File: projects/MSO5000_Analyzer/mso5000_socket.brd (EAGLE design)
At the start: 76.7 x 38 mm, 3 parts

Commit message: Editing board
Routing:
- net !D4: track 63.4 -> 64.9 mm
- net !D5: track 65.3 -> 66.5 mm
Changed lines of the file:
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@@
 <wire x1="74.9" y1="40.5" x2="-1.3" y2="40.5" width="0" layer="20"/>
 <wire x1="-1.3" y1="40.5" x2="-1.79" y2="2.47" width="0" layer="20"/>
-<wire x1="22.7" y1="10.2" x2="22.7" y2="12.9" width="0.1524" layer="41"/>
-<wire x1="22.7" y1="12.9" x2="20.7" y2="12.9" width="0.1524" layer="41"/>
-<wire x1="20.7" y1="12.9" x2="20.7" y2="10.2" width="0.1524" layer="41"/>
-<wire x1="50.9" y1="10.1" x2="50.9" y2="12.8" width="0.1524" layer="41"/>
-<wire x1="50.9" y1="12.8" x2="48.9" y2="12.8" width="0.1524" layer="41"/>
-<wire x1="48.9" y1="12.8" x2="48.9" y2="10.1" width="0.1524" layer="41"/>
+<wire x1="22.7" y1="12.2" x2="20.7" y2="12.2" width="0.1524" layer="41"/>
+<wire x1="50.6" y1="12.2" x2="48.6" y2="12.2" width="0.1524" layer="41"/>
+<wire x1="20.7" y1="12.2" x2="20.7" y2="8.7" width="0.1524" layer="41"/>
+<wire x1="22.7" y1="12.2" x2="22.7" y2="8.7" width="0.1524" layer="41"/>
+<wire x1="48.6" y1="12.2" x2="48.6" y2="8.8" width="0.1524" layer="41"/>
+<wire x1="50.6" y1="12.2" x2="50.6" y2="8.8" width="0.1524" layer="41"/>
 </plain>
 <attributes>
@@
 <wire x1="30.06" y1="8.06" x2="30.06" y2="8.59699375" width="0.254" layer="1"/>
 <wire x1="30.06" y1="8.59699375" x2="30.06" y2="11.43" width="0.254" layer="1"/>
-<wire x1="19.5" y1="12.62591875" x2="19.5" y2="9.6" width="0.254" layer="16"/>
+<wire x1="19.5" y1="12.62591875" x2="19.5" y2="7.5" width="0.254" layer="16"/>
 <wire x1="18.05611875" y1="31.1302" x2="20.64388125" y2="31.1302" width="0.254" layer="16"/>
 <wire x1="17.4698" y1="30.54388125" x2="18.05611875" y2="31.1302" width="0.254" layer="16"/>
@@
 <wire x1="21.01439375" y1="30.7596875" x2="20.64388125" y2="31.1302" width="0.254" layer="16"/>
 <wire x1="19.5" y1="12.62591875" x2="22.087040625" y2="15.212959375" width="0.254" layer="16"/>
-<wire x1="19.5" y1="9.6" x2="22.4948875" y2="6.6051125" width="0.254" layer="16"/>
-<wire x1="22.4948875" y1="6.6051125" x2="27.4051125" y2="6.6051125" width="0.254" layer="16"/>
+<wire x1="19.5" y1="7.5" x2="20.3948875" y2="6.6051125" width="0.254" layer="16"/>
+<wire x1="20.3948875" y1="6.6051125" x2="27.4051125" y2="6.6051125" width="0.254" layer="16"/>
 <wire x1="22.087040625" y1="15.212959375" x2="22.087040625" y2="25.153634375" width="0.254" layer="16"/>
 <wire x1="22.087040625" y1="25.153634375" x2="18.436475" y2="28.8042" width="0.254" layer="16"/>
@@
 <wire x1="20.8" y1="15.3" x2="20.375734375" y2="14.875734375" width="0.254" layer="1"/>
 <wire x1="20.375734375" y1="14.875734375" x2="19.3" y2="13.8" width="0.254" layer="1"/>
-<wire x1="19.3" y1="13.8" x2="19.3" y2="9.8" width="0.254" layer="1"/>
+<wire x1="19.3" y1="13.8" x2="19.3" y2="7.3" width="0.254" layer="1"/>
 <wire x1="29.06" y1="8.66" x2="29.06" y2="11.43" width="0.254" layer="1"/>
 <wire x1="24.13" y1="34.43" x2="22.9" y2="33.2" width="0.254" layer="16"/>
 <wire x1="16.9958" y1="30.84021875" x2="16.9958" y2="28.9042" width="0.254" layer="16"/>
-<wire x1="19.3" y1="9.8" x2="23.0948875" y2="6.0051125" width="0.254" layer="1"/>
-<wire x1="23.0948875" y1="6.0051125" x2="26.4051125" y2="6.0051125" width="0.254" layer="1"/>
+<wire x1="19.3" y1="7.3" x2="20.5948875" y2="6.0051125" width="0.254" layer="1"/>
+<wire x1="20.5948875" y1="6.0051125" x2="26.4051125" y2="6.0051125" width="0.254" layer="1"/>
 <wire x1="26.4051125" y1="6.0051125" x2="29.06" y2="8.66" width="0.254" layer="1"/>
 <wire x1="21.6" y1="24.8703375" x2="21.6" y2="16.1" width="0.254" layer="16"/>

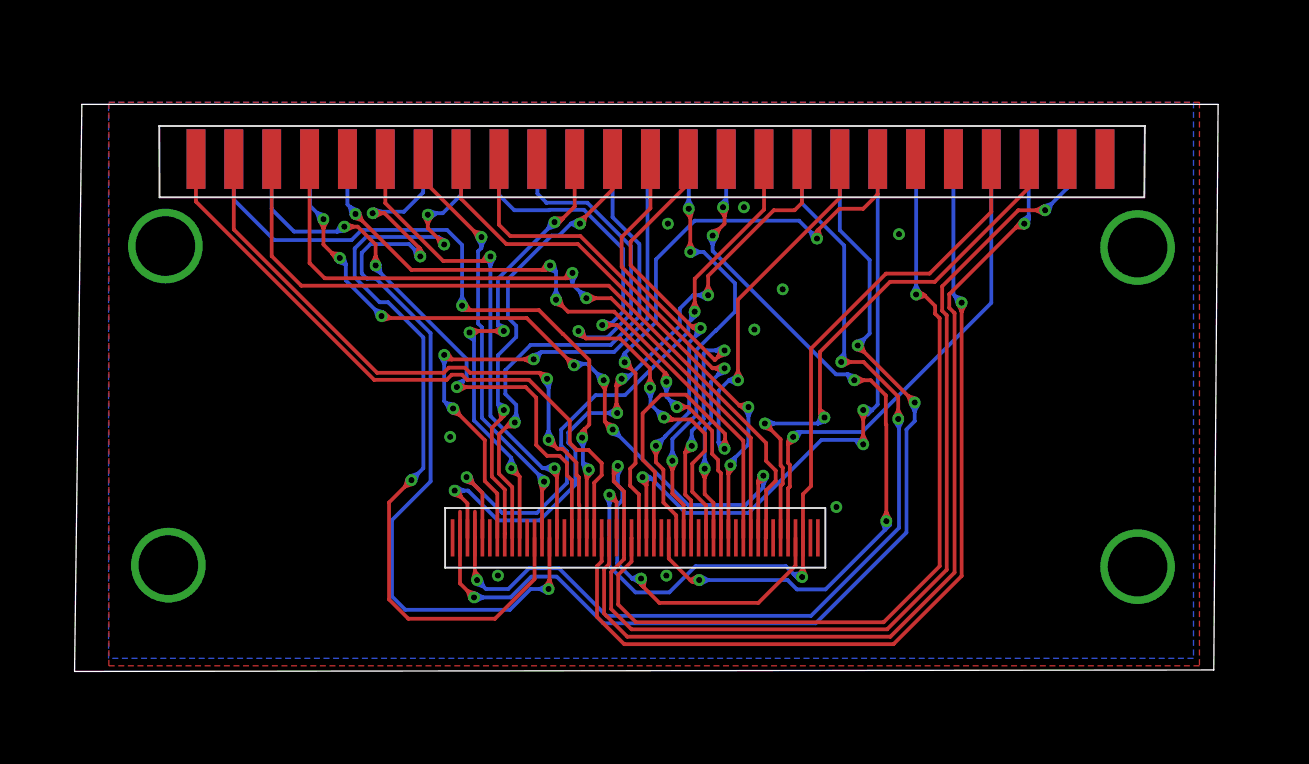
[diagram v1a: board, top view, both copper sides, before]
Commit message: Editing Area Top and Bottom. Adding extra calibration point's
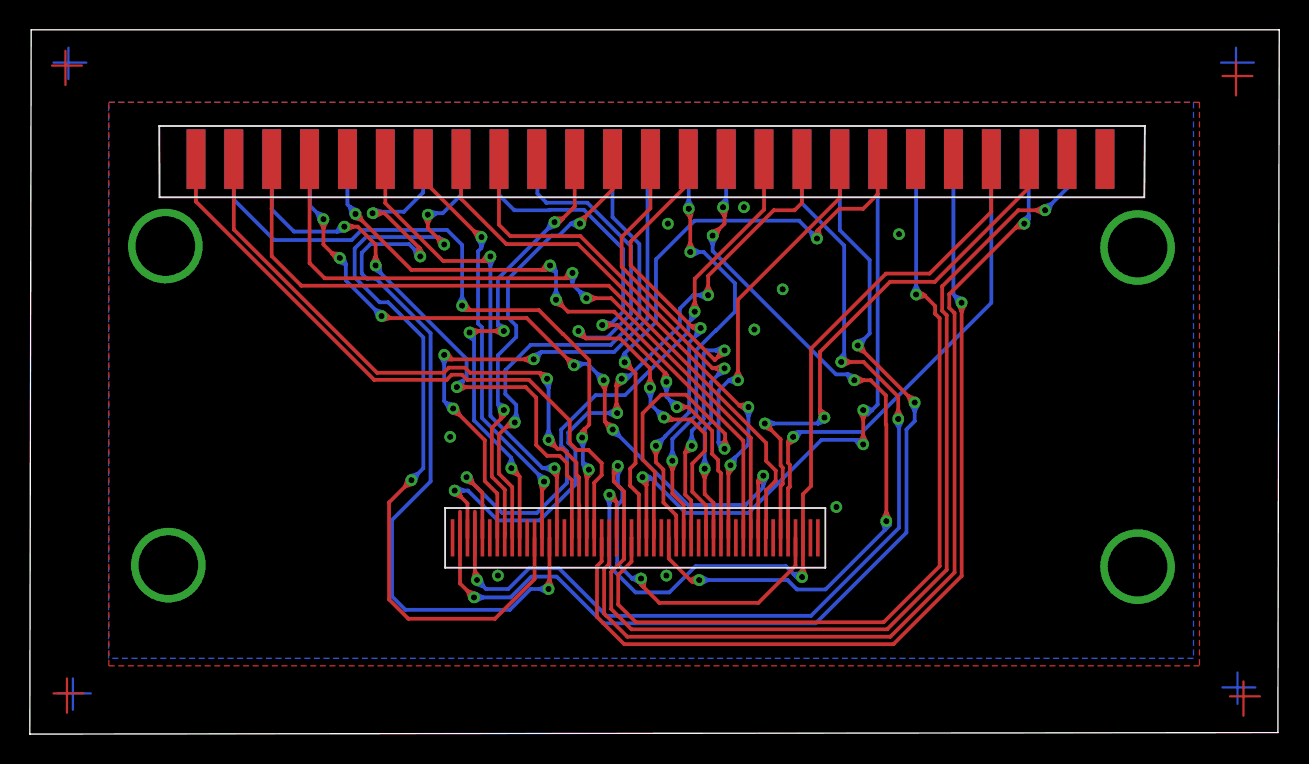
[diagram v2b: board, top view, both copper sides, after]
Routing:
- net N$5: track 0.00 -> 2.30 mm
- net N$9: track 0.00 -> 2.30 mm
- net N$11: track 0.00 -> 2.30 mm
- net N$7: track 0.00 -> 2.30 mm
- net N$18: track 0.00 -> 2.20 mm
- net N$16: track 0.00 -> 2.20 mm
- net N$20: track 0.00 -> 2.20 mm
- net N$14: track 0.00 -> 2.20 mm
- net N$19: track 0.00 -> 2.10 mm
- net N$17: track 0.00 -> 2.10 mm
- net N$15: track 0.00 -> 2.10 mm
- net N$13: track 0.00 -> 2.10 mm
- net N$8: track 0.00 -> 2.00 mm
- net N$12: track 0.00 -> 2.00 mm
- net N$10: track 0.00 -> 2.00 mm
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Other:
- board size 76.7 x 38 mm -> 83.8 x 47.2 mm
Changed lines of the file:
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@@
 <grid distance="0.1" unitdist="mm" unit="mm" style="lines" multiple="1" display="no" altdistance="0.01" altunitdist="mm" altunit="mm"/>
 <layers>
-<layer number="1" name="Top" color="4" fill="1" visible="yes" active="yes"/>
+<layer number="1" name="Top" color="4" fill="1" visible="no" active="yes"/>
 <layer number="2" name="Route2" color="16" fill="1" visible="no" active="no"/>
 <layer number="3" name="Route3" color="17" fill="1" visible="no" active="no"/>
@@
 <board>
 <plain>
-<wire x1="-1.79" y1="2.47" x2="74.61" y2="2.57" width="0" layer="20"/>
-<wire x1="74.61" y1="2.57" x2="74.9" y2="40.5" width="0" layer="20"/>
-<wire x1="74.9" y1="40.5" x2="-1.3" y2="40.5" width="0" layer="20"/>
-<wire x1="-1.3" y1="40.5" x2="-1.79" y2="2.47" width="0" layer="20"/>
+<wire x1="-4.79" y1="-1.73" x2="78.91" y2="-1.63" width="0" layer="20"/>
+<wire x1="78.91" y1="-1.63" x2="79" y2="45.5" width="0" layer="20"/>
+<wire x1="79" y1="45.5" x2="-4.7" y2="45.5" width="0" layer="20"/>
+<wire x1="-4.7" y1="45.5" x2="-4.79" y2="-1.73" width="0" layer="20"/>
 <wire x1="22.7" y1="12.2" x2="20.7" y2="12.2" width="0.1524" layer="41"/>
 <wire x1="50.6" y1="12.2" x2="48.6" y2="12.2" width="0.1524" layer="41"/>
@@
 <via x="69.5" y="30.9" extent="1-16" drill="4"/>
 </signal>
+<signal name="N$7">
+<wire x1="76.1" y1="43.4" x2="76.1" y2="41.1" width="0.1524" layer="1"/>
+</signal>
+<signal name="N$8">
+<wire x1="75.2" y1="42.4" x2="77.2" y2="42.4" width="0.1524" layer="1"/>
+</signal>
+<signal name="N$9">
+<wire x1="-2.3" y1="2" x2="-2.3" y2="-0.3" width="0.1524" layer="1"/>
+</signal>
+<signal name="N$10">
+<wire x1="-3.2" y1="1" x2="-1.2" y2="1" width="0.1524" layer="1"/>
+</signal>
+<signal name="N$11">
+<wire x1="76.6" y1="1.8" x2="76.6" y2="-0.5" width="0.1524" layer="1"/>
+</signal>
+<signal name="N$12">
+<wire x1="75.7" y1="0.8" x2="77.7" y2="0.8" width="0.1524" layer="1"/>
+</signal>
+<signal name="N$5">
+<wire x1="-2.4" y1="44.1" x2="-2.4" y2="41.8" width="0.1524" layer="1"/>
+</signal>
+<signal name="N$6">
+<wire x1="-3.3" y1="43.1" x2="-1.3" y2="43.1" width="0.1524" layer="1"/>
+</signal>
+<signal name="N$15">
+<wire x1="76.1" y1="44.3" x2="76.1" y2="42.2" width="0.1524" layer="16"/>
+</signal>
+<signal name="N$16">
+<wire x1="75.1" y1="43.3" x2="77.3" y2="43.3" width="0.1524" layer="16"/>
+</signal>
+<signal name="N$17">
+<wire x1="76.2" y1="2.4" x2="76.2" y2="0.3" width="0.1524" layer="16"/>
+</signal>
+<signal name="N$18">
+<wire x1="75.2" y1="1.4" x2="77.4" y2="1.4" width="0.1524" layer="16"/>
+</signal>
+<signal name="N$19">
+<wire x1="-1.9" y1="2" x2="-1.9" y2="-0.1" width="0.1524" layer="16"/>
+</signal>
+<signal name="N$20">
+<wire x1="-2.9" y1="1" x2="-0.7" y2="1" width="0.1524" layer="16"/>
+</signal>
+<signal name="N$13">
+<wire x1="-2.2" y1="44.3" x2="-2.2" y2="42.2" width="0.1524" layer="16"/>
+</signal>
+<signal name="N$14">
+<wire x1="-3.2" y1="43.3" x2="-1" y2="43.3" width="0.1524" layer="16"/>
+</signal>
 </signals>
 <mfgpreviewcolors>
@@
 <mfgpreviewcolor name="substratecolor" color="0xFF786E46"/>
 </mfgpreviewcolors>
+<errors>
+</errors>
 </board>
 </drawing>

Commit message: Editing board
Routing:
- net N$5: track 2.30 -> 0.00 mm
- net N$9: track 2.30 -> 0.00 mm
- net N$11: track 2.30 -> 0.00 mm
- net N$7: track 2.30 -> 0.00 mm
- net N$18: track 2.20 -> 0.00 mm
- net N$16: track 2.20 -> 0.00 mm
- net N$20: track 2.20 -> 0.00 mm
- net N$14: track 2.20 -> 0.00 mm
- net N$19: track 2.10 -> 0.00 mm
- net N$17: track 2.10 -> 0.00 mm
- net N$15: track 2.10 -> 0.00 mm
- net N$13: track 2.10 -> 0.00 mm
- net N$8: track 2.00 -> 0.00 mm
- net N$12: track 2.00 -> 0.00 mm
- net N$10: track 2.00 -> 0.00 mm
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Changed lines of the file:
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@@
 <grid distance="0.1" unitdist="mm" unit="mm" style="lines" multiple="1" display="no" altdistance="0.01" altunitdist="mm" altunit="mm"/>
 <layers>
-<layer number="1" name="Top" color="4" fill="1" visible="no" active="yes"/>
+<layer number="1" name="Top" color="4" fill="1" visible="yes" active="yes"/>
 <layer number="2" name="Route2" color="16" fill="1" visible="no" active="no"/>
 <layer number="3" name="Route3" color="17" fill="1" visible="no" active="no"/>
@@
 <via x="69.5" y="30.9" extent="1-16" drill="4"/>
 </signal>
-<signal name="N$7">
-<wire x1="76.1" y1="43.4" x2="76.1" y2="41.1" width="0.1524" layer="1"/>
-</signal>
-<signal name="N$8">
-<wire x1="75.2" y1="42.4" x2="77.2" y2="42.4" width="0.1524" layer="1"/>
-</signal>
-<signal name="N$9">
-<wire x1="-2.3" y1="2" x2="-2.3" y2="-0.3" width="0.1524" layer="1"/>
-</signal>
-<signal name="N$10">
-<wire x1="-3.2" y1="1" x2="-1.2" y2="1" width="0.1524" layer="1"/>
-</signal>
-<signal name="N$11">
-<wire x1="76.6" y1="1.8" x2="76.6" y2="-0.5" width="0.1524" layer="1"/>
-</signal>
-<signal name="N$12">
-<wire x1="75.7" y1="0.8" x2="77.7" y2="0.8" width="0.1524" layer="1"/>
-</signal>
-<signal name="N$5">
-<wire x1="-2.4" y1="44.1" x2="-2.4" y2="41.8" width="0.1524" layer="1"/>
-</signal>
-<signal name="N$6">
-<wire x1="-3.3" y1="43.1" x2="-1.3" y2="43.1" width="0.1524" layer="1"/>
-</signal>
-<signal name="N$15">
-<wire x1="76.1" y1="44.3" x2="76.1" y2="42.2" width="0.1524" layer="16"/>
-</signal>
-<signal name="N$16">
-<wire x1="75.1" y1="43.3" x2="77.3" y2="43.3" width="0.1524" layer="16"/>
-</signal>
-<signal name="N$17">
-<wire x1="76.2" y1="2.4" x2="76.2" y2="0.3" width="0.1524" layer="16"/>
-</signal>
-<signal name="N$18">
-<wire x1="75.2" y1="1.4" x2="77.4" y2="1.4" width="0.1524" layer="16"/>
-</signal>
-<signal name="N$19">
-<wire x1="-1.9" y1="2" x2="-1.9" y2="-0.1" width="0.1524" layer="16"/>
-</signal>
-<signal name="N$20">
-<wire x1="-2.9" y1="1" x2="-0.7" y2="1" width="0.1524" layer="16"/>
-</signal>
-<signal name="N$13">
-<wire x1="-2.2" y1="44.3" x2="-2.2" y2="42.2" width="0.1524" layer="16"/>
-</signal>
-<signal name="N$14">
-<wire x1="-3.2" y1="43.3" x2="-1" y2="43.3" width="0.1524" layer="16"/>
-</signal>
 </signals>
